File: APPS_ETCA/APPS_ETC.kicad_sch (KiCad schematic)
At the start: 20 parts, among them P1 DTM1312PC12PDR008, U1 NUCLEO-L432KC, U2 MCP6004, U6 LM7805_TO220, U8 LM7809_TO220

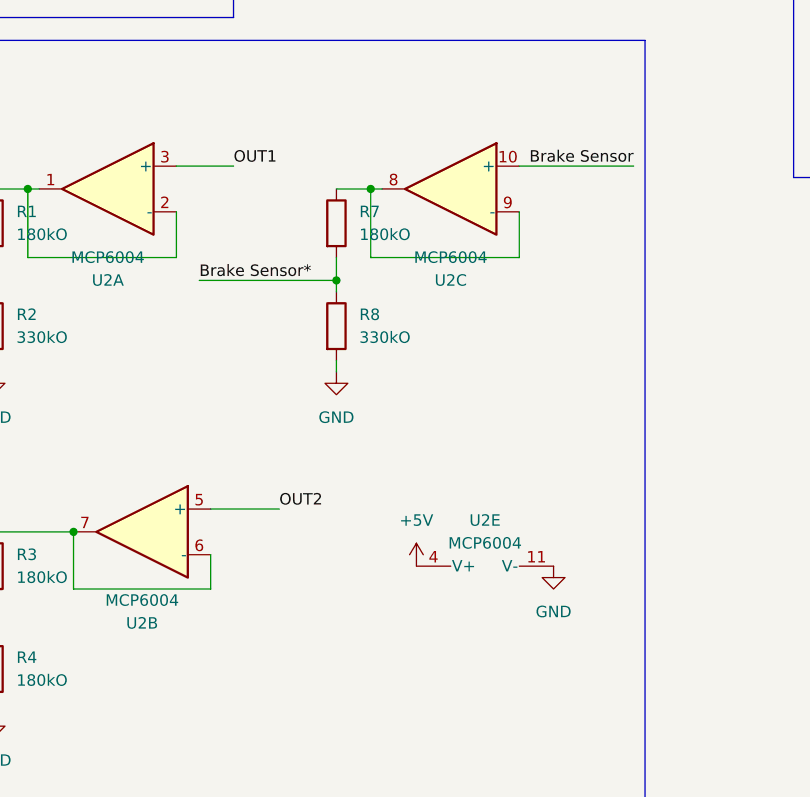
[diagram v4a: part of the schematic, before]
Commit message: 100k Pull down resistor for all inputs to MCU pre- opamp
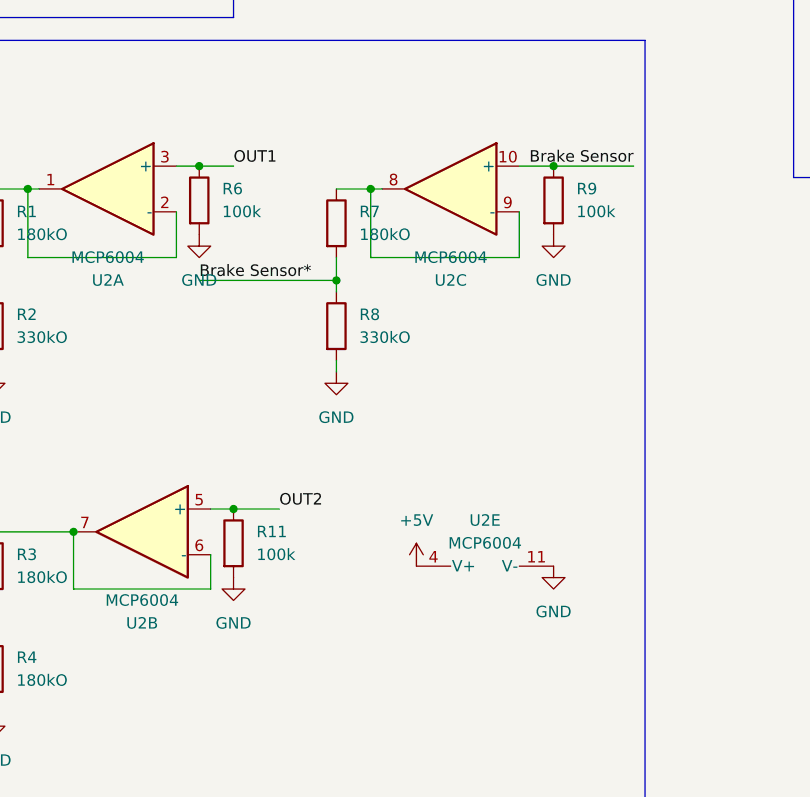
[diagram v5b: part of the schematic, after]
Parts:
- added R11, R6, R9: 100k, Resistor_SMD:R_0805_2012Metric_Pad1.20x1.40mm_HandSolder, symbol Device:R
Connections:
- net Brake Sensor: now also R9.1
- net GND: now also R11.2, R6.2, R9.2
- net OUT1: now also R6.1
- net OUT2: now also R11.1
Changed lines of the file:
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@@
   (junction (at 181.61 66.04) (diameter 0) (color 0 0 0 0)
   )
+  (junction (at 162.56 63.5) (diameter 0) (color 0 0 0 0)
+  )
   (junction (at 38.1 102.87) (diameter 0) (color 0 0 0 0)
   )
@@
   (junction (at 58.42 39.37) (diameter 0) (color 0 0 0 0)
   )
+  (junction (at 166.37 101.6) (diameter 0) (color 0 0 0 0)
+  )
   (junction (at 73.66 25.4) (diameter 0) (color 0 0 0 0)
   )
+  (junction (at 201.93 63.5) (diameter 0) (color 0 0 0 0)
+  )
   (junction (at 143.51 66.04) (diameter 0) (color 0 0 0 0)
   )
@@
     (stroke (width 0) (type default))
   )
-  (wire (pts (xy 163.83 101.6) (xy 171.45 101.6))
+  (wire (pts (xy 163.83 101.6) (xy 166.37 101.6))
     (stroke (width 0) (type default))
   )
@@
     (stroke (width 0) (type default))
   )
+  (wire (pts (xy 162.56 63.5) (xy 166.37 63.5))
+    (stroke (width 0) (type default))
+  )
   (wire (pts (xy 242.57 17.78) (xy 242.57 24.13))
     (stroke (width 0) (type default))
@@
     (stroke (width 0) (type default))
   )
+  (wire (pts (xy 160.02 63.5) (xy 162.56 63.5))
+    (stroke (width 0) (type default))
+  )
   (wire (pts (xy 114.3 30.48) (xy 120.65 30.48))
     (stroke (width 0) (type default))
@@
     (stroke (width 0) (type default))
   )
-  (wire (pts (xy 160.02 63.5) (xy 166.37 63.5))
-    (stroke (width 0) (type default))
-  )
   (wire (pts (xy 139.7 111.76) (xy 139.7 114.3))
     (stroke (width 0) (type default))
@@
     (stroke (width 0) (type default))
   )
-  (wire (pts (xy 198.12 63.5) (xy 210.82 63.5))
-    (stroke (width 0) (type default))
-  )
   (wire (pts (xy 73.66 22.86) (xy 73.66 25.4))
     (stroke (width 0) (type default))
@@
     (stroke (width 0) (type default))
   )
+  (wire (pts (xy 201.93 63.5) (xy 210.82 63.5))
+    (stroke (width 0) (type default))
+  )
   (wire (pts (xy 245.11 17.78) (xy 245.11 24.13))
     (stroke (width 0) (type default))
@@
     (stroke (width 0) (type default))
   )
+  (wire (pts (xy 166.37 101.6) (xy 171.45 101.6))
+    (stroke (width 0) (type default))
+  )
   (wire (pts (xy 26.67 102.87) (xy 38.1 102.87))
+    (stroke (width 0) (type default))
+  )
+  (wire (pts (xy 198.12 63.5) (xy 201.93 63.5))
     (stroke (width 0) (type default))
   )
@@
         (path "/21da8b0a-bf7f-4003-9579-5de7190091be"
           (reference "#PWR014") (unit 1)
+        )
+      )
+    )
+  )
+  (symbol (lib_id "power:GND") (at 166.37 109.22 0) (unit 1)
+    (in_bom yes) (on_board yes) (dnp no) (fields_autoplaced)
+    (property "Reference" "#PWR033" (at 166.37 115.57 0)
+      (effects (font (size 1.27 1.27)) hide)
+    )
+    (property "Value" "GND" (at 166.37 114.3 0)
+      (effects (font (size 1.27 1.27)))
+    )
+    (property "Footprint" "" (at 166.37 109.22 0)
+      (effects (font (size 1.27 1.27)) hide)
+    )
+    (property "Datasheet" "" (at 166.37 109.22 0)
+      (effects (font (size 1.27 1.27)) hide)
+    )
+    (pin "1")
+    (instances
+      (project "APPS_ETC"
+        (path "/21da8b0a-bf7f-4003-9579-5de7190091be"
+          (reference "#PWR033") (unit 1)
         )
       )
@@
     )
   )
+  (symbol (lib_id "Device:R") (at 162.56 67.31 0) (unit 1)
+    (in_bom yes) (on_board yes) (dnp no) (fields_autoplaced)
+    (property "Reference" "R6" (at 165.1 66.04 0)
+      (effects (font (size 1.27 1.27)) (justify left))
+    )
+    (property "Value" "100k" (at 165.1 68.58 0)
+      (effects (font (size 1.27 1.27)) (justify left))
+    )
+    (property "Footprint" "Resistor_SMD:R_0805_2012Metric_Pad1.20x1.40mm_HandSolder" (at 160.782 67.31 90)
+      (effects (font (size 1.27 1.27)) hide)
+    )
+    (property "Datasheet" "~" (at 162.56 67.31 0)
+      (effects (font (size 1.27 1.27)) hide)
+    )
+    (pin "1")
+    (pin "2")
+    (instances
+      (project "APPS_ETC"
+        (path "/21da8b0a-bf7f-4003-9579-5de7190091be"
+          (reference "R6") (unit 1)
+        )
+      )
+    )
+  )
   (symbol (lib_id "1FS_2_Global_Symbol_Library:STS6NF20V") (at 17.78 36.83 0) (unit 1)
     (in_bom yes) (on_board yes) (dnp no) (fields_autoplaced)
@@
     )
   )
+  (symbol (lib_id "Device:R") (at 166.37 105.41 0) (unit 1)
+    (in_bom yes) (on_board yes) (dnp no) (fields_autoplaced)
+    (property "Reference" "R11" (at 168.91 104.14 0)
+      (effects (font (size 1.27 1.27)) (justify left))
+    )
+    (property "Value" "100k" (at 168.91 106.68 0)
+      (effects (font (size 1.27 1.27)) (justify left))
+    )
+    (property "Footprint" "Resistor_SMD:R_0805_2012Metric_Pad1.20x1.40mm_HandSolder" (at 164.592 105.41 90)
+      (effects (font (size 1.27 1.27)) hide)
+    )
+    (property "Datasheet" "~" (at 166.37 105.41 0)
+      (effects (font (size 1.27 1.27)) hide)
+    )
+    (pin "1")
+    (pin "2")
+    (instances
+      (project "APPS_ETC"
+        (path "/21da8b0a-bf7f-4003-9579-5de7190091be"
+          (reference "R11") (unit 1)
+        )
+      )
+    )
+  )
   (symbol (lib_id "power:+12V") (at 43.18 66.04 0) (unit 1)
     (in_bom yes) (on_board yes) (dnp no) (fields_autoplaced)
@@
         (path "/21da8b0a-bf7f-4003-9579-5de7190091be"
           (reference "R2") (unit 1)
+        )
+      )
+    )
+  )
+  (symbol (lib_id "power:GND") (at 201.93 71.12 0) (unit 1)
+    (in_bom yes) (on_board yes) (dnp no) (fields_autoplaced)
+    (property "Reference" "#PWR031" (at 201.93 77.47 0)
+      (effects (font (size 1.27 1.27)) hide)
+    )
+    (property "Value" "GND" (at 201.93 76.2 0)
+      (effects (font (size 1.27 1.27)))
+    )
+    (property "Footprint" "" (at 201.93 71.12 0)
+      (effects (font (size 1.27 1.27)) hide)
+    )
+    (property "Datasheet" "" (at 201.93 71.12 0)
+      (effects (font (size 1.27 1.27)) hide)
+    )
+    (pin "1")
+    (instances
+      (project "APPS_ETC"
+        (path "/21da8b0a-bf7f-4003-9579-5de7190091be"
+          (reference "#PWR031") (unit 1)
         )
       )
@@
     )
   )
+  (symbol (lib_id "power:GND") (at 162.56 71.12 0) (unit 1)
+    (in_bom yes) (on_board yes) (dnp no) (fields_autoplaced)
+    (property "Reference" "#PWR027" (at 162.56 77.47 0)
+      (effects (font (size 1.27 1.27)) hide)
+    )
+    (property "Value" "GND" (at 162.56 76.2 0)
+      (effects (font (size 1.27 1.27)))
+    )
+    (property "Footprint" "" (at 162.56 71.12 0)
+      (effects (font (size 1.27 1.27)) hide)
+    )
+    (property "Datasheet" "" (at 162.56 71.12 0)
+      (effects (font (size 1.27 1.27)) hide)
+    )
+    (pin "1")
+    (instances
+      (project "APPS_ETC"
+        (path "/21da8b0a-bf7f-4003-9579-5de7190091be"
+          (reference "#PWR027") (unit 1)
+        )
+      )
+    )
+  )
   (symbol (lib_id "power:GND") (at 76.2 68.58 270) (unit 1)
     (in_bom yes) (on_board yes) (dnp no) (fields_autoplaced)
@@
         )
       )
+    )
+  )
+  (symbol (lib_id "Device:R") (at 201.93 67.31 0) (unit 1)
+    (in_bom yes) (on_board yes) (dnp no) (fields_autoplaced)
+    (property "Reference" "R9" (at 204.47 66.04 0)
+      (effects (font (size 1.27 1.27)) (justify left))
+    )
+    (property "Value" "100k" (at 204.47 68.58 0)
+      (effects (font (size 1.27 1.27)) (justify left))
+    )
+    (property "Footprint" "Resistor_SMD:R_0805_2012Metric_Pad1.20x1.40mm_HandSolder" (at 200.152 67.31 90)
+      (effects (font (size 1.27 1.27)) hide)
+    )
+    (property "Datasheet" "~" (at 201.93 67.31 0)
+      (effects (font (size 1.27 1.27)) hide)
+    )
+    (pin "1")
+    (pin "2")
+    (instances
+      (project "APPS_ETC"
+        (path "/21da8b0a-bf7f-4003-9579-5de7190091be"
+          (reference "R9") (unit 1)
+        )
+      )

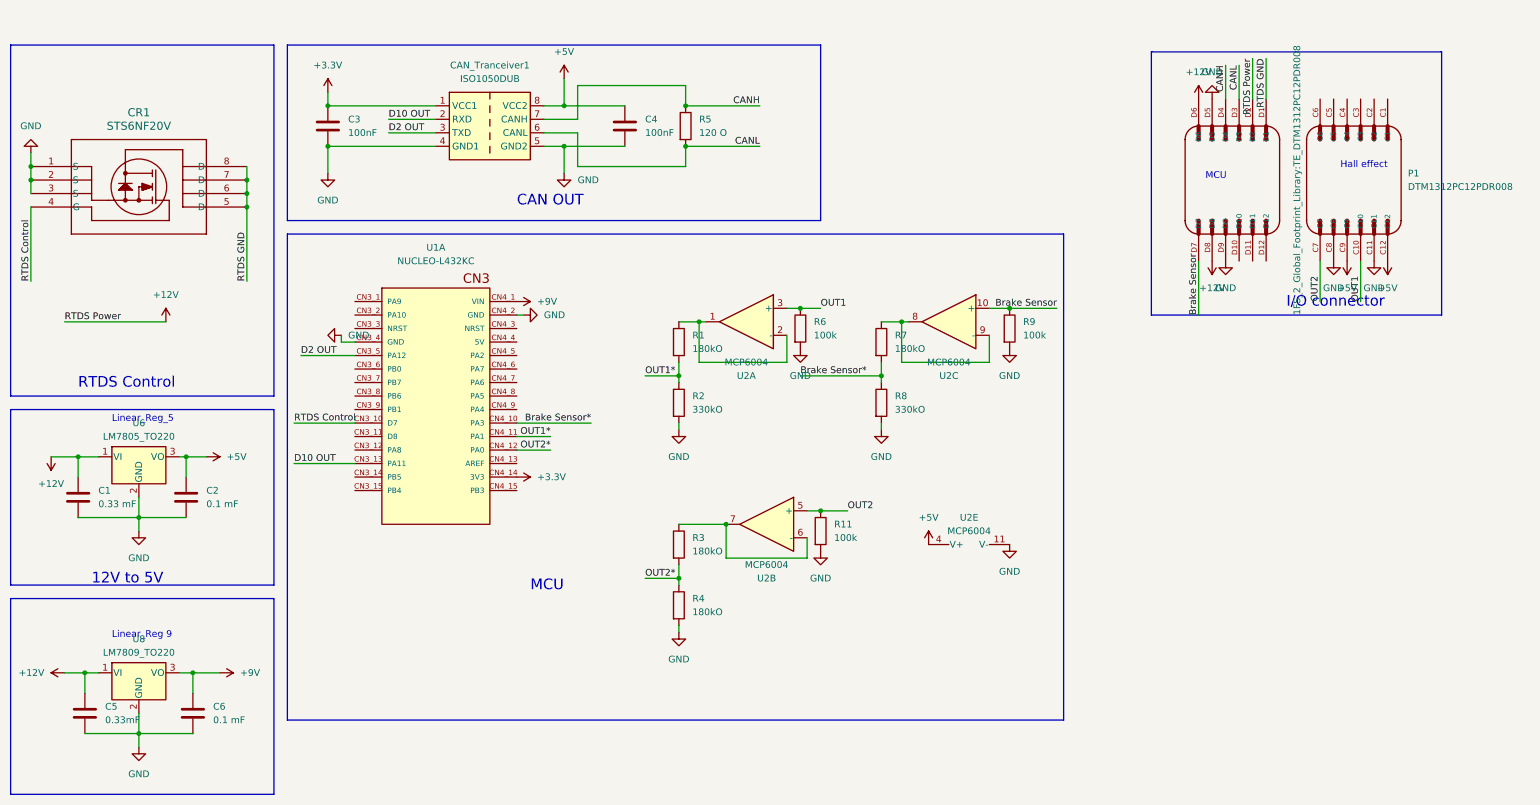
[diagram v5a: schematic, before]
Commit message: Add decoupling capacitor to analog inputs. 40 nF for 50 hz sample rate.
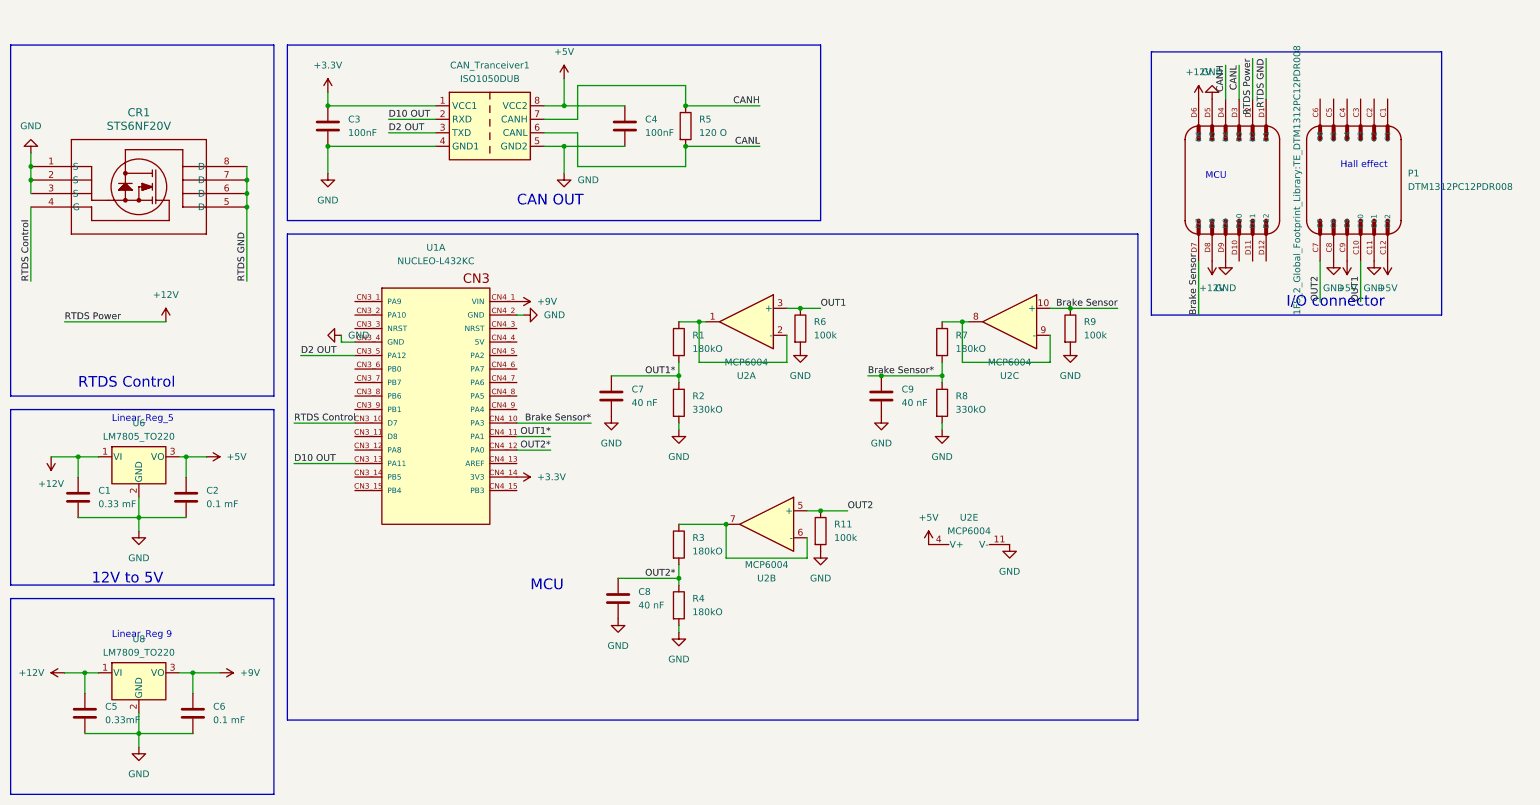
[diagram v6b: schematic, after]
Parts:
- added C7, C8, C9: 40 nF, Capacitor_SMD:C_0805_2012Metric_Pad1.18x1.45mm_HandSolder, symbol Device:C
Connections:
- net Brake Sensor*: now also C9.1
- net GND: now also C7.2, C8.2, C9.2
- net OUT1*: now also C7.1
- net OUT2*: now also C8.1
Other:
- moved on the sheet: R7, R8, R9, U2C

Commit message: cockpit in, rtds control, and 3.3v and organized.
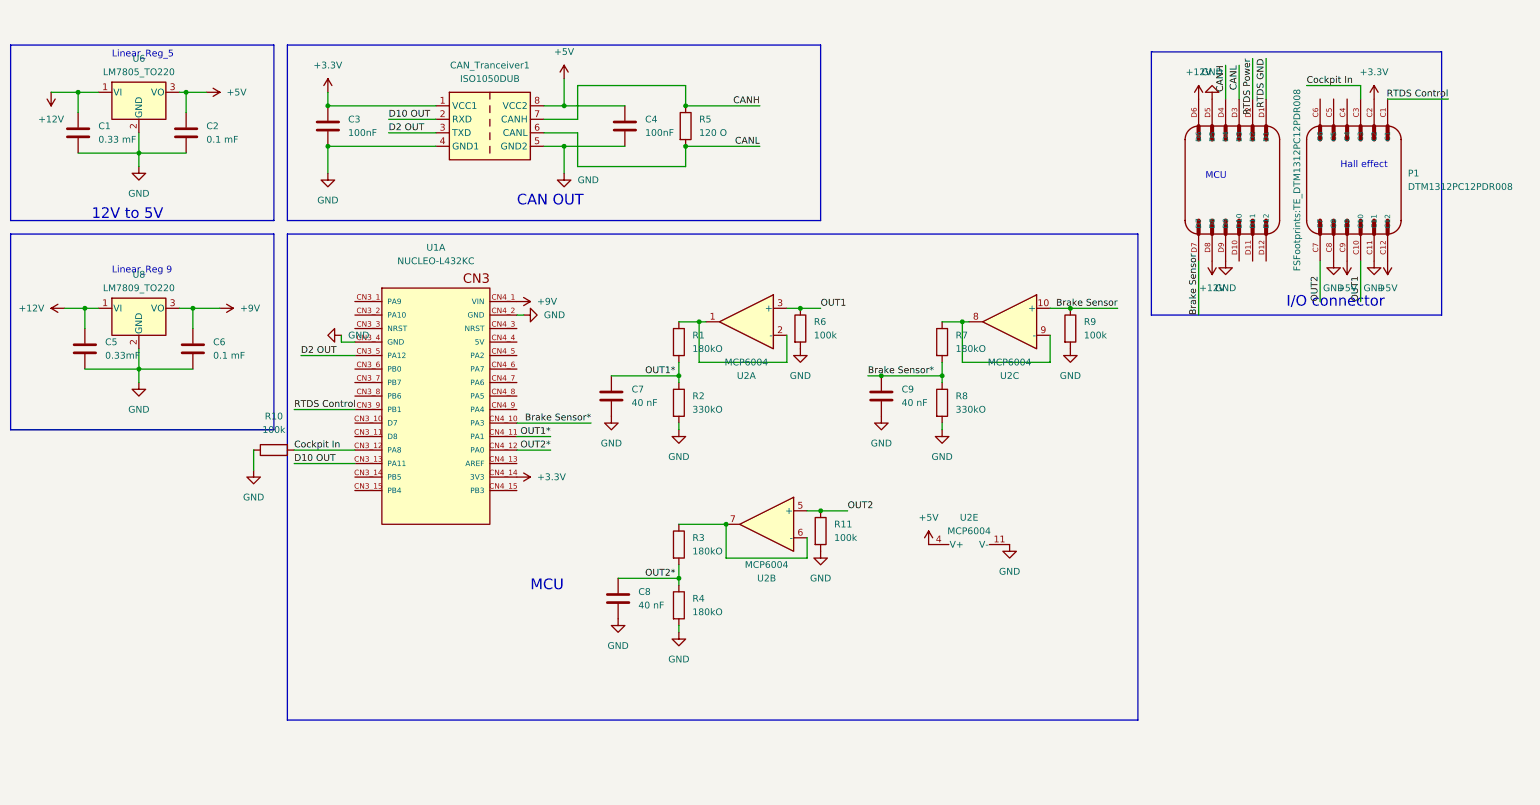
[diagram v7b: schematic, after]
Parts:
- removed CR1: STS6NF20V, 1FS_2_Global_Footprint_Library:SOIC127P600X175-8N, symbol 1FS_2_Global_Symbol_Library:STS6NF20V
- added R10: 100k, Resistor_SMD:R_0805_2012Metric_Pad1.20x1.40mm_HandSolder, symbol Device:R
- P1: footprint 1FS_2_Global_Footprint_Library:TE_DTM1312PC12PDR008 -> FSFootprints:TE_DTM1312PC12PDR008
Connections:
- net +12V: no longer P1.D2
- net +3.3V: now also P1.C2
- net GND: now also R10.1
- net RTDS Control: now also P1.C1, U1.CN3_9 (PB1); no longer U1.CN3_10 (D7)
- net Cockpit In: now reaches P1.C3
- net Cockpit In: now also U1.CN3_12 (PA8), R10.2
- new net RTDS Power: P1.D2
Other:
- note removed: "RTDS Control"
- moved on the sheet: C1, C2, C5, C6, U6, U8

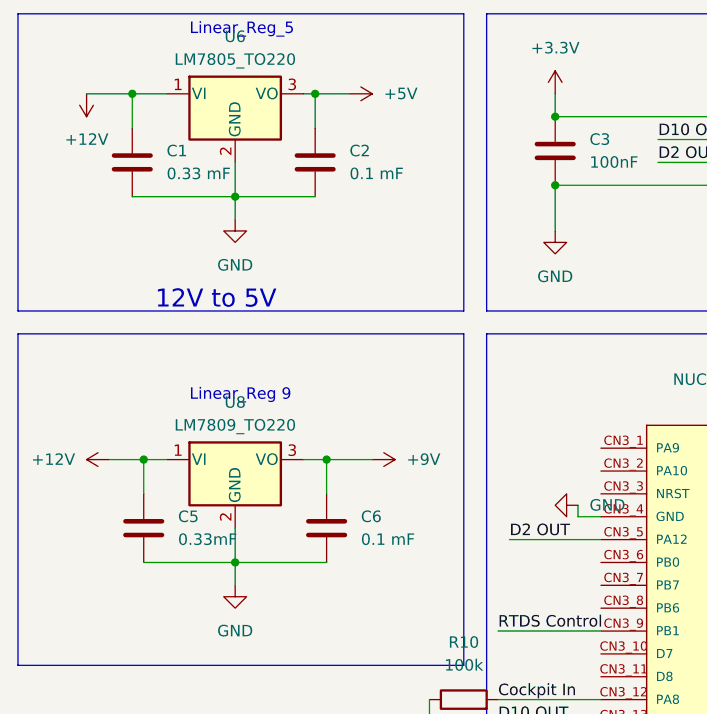
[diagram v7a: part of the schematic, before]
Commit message: Replaced all mf with micro farad
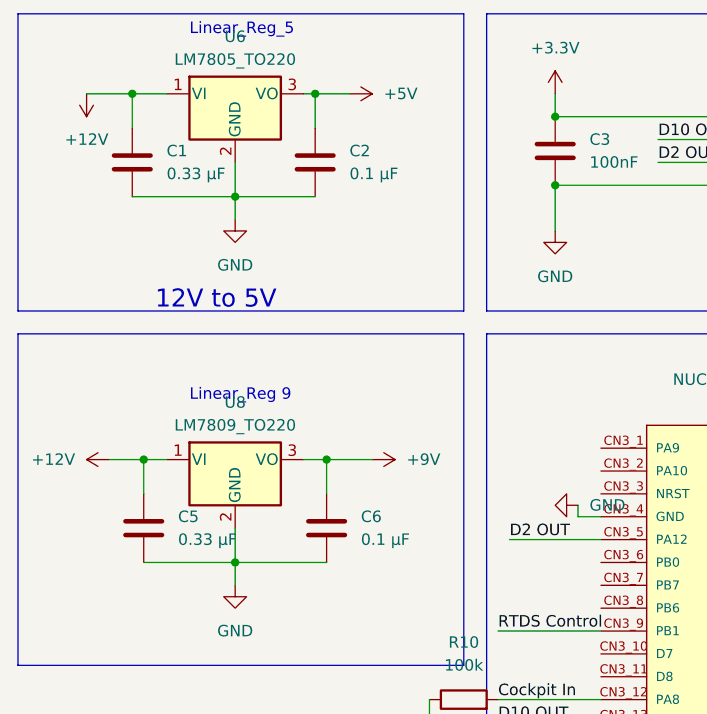
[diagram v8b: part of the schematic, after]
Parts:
- C1: value 0.33 mF -> 0.33 µF
- C2, C6: value 0.1 mF -> 0.1 µF
- C5: value 0.33mF -> 0.33 µF
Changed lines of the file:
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@@
       (effects (font (size 1.27 1.27)) (justify left))
     )
-    (property "Value" "0.1 mF" (at 50.8 31.75 0)
+    (property "Value" "0.1 µF" (at 50.8 31.75 0)
       (effects (font (size 1.27 1.27)) (justify left))
     )
@@
       (effects (font (size 1.27 1.27)) (justify left))
     )
-    (property "Value" "0.33 mF" (at 30.48 31.75 0)
+    (property "Value" "0.33 µF" (at 30.48 31.75 0)
       (effects (font (size 1.27 1.27)) (justify left))
     )
@@
       (effects (font (size 1.27 1.27)) (justify left))
     )
-    (property "Value" "0.33mF" (at 31.75 72.39 0)
+    (property "Value" "0.33 µF" (at 31.75 72.39 0)
       (effects (font (size 1.27 1.27)) (justify left))
     )
@@
       (effects (font (size 1.27 1.27)) (justify left))
     )
-    (property "Value" "0.1 mF" (at 52.07 72.39 0)
-      (effects (font (size 1.27 1.27)) (justify left))
-    )
+    (property "Value" "0.1 µF" (at 52.07 72.39 0)
+      (effects (font (size 1.27 1.27)) (justify left))
+    )
